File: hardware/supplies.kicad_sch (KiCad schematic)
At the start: 7 parts, among them U301 LM7805_TO220

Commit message: Added analog stage for Vbat measurement, and it's simulation
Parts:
- F301: footprint Fuse:Fuse_1812_4532Metric_Pad1.30x3.40mm_HandSolder -> Fuse:Fuse_1206_3216Metric_Pad1.42x1.75mm_HandSolder
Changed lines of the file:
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@@
     (property "Reference" "F301" (id 0) (at 119.38 95.8682 90))
     (property "Value" "Fuse" (id 1) (at 119.38 98.4051 90))
-    (property "Footprint" "Fuse:Fuse_1812_4532Metric_Pad1.30x3.40mm_HandSolder" (id 2) (at 119.38 102.108 90)
+    (property "Footprint" "Fuse:Fuse_1206_3216Metric_Pad1.42x1.75mm_HandSolder" (id 2) (at 119.38 102.108 90)
       (effects (font (size 1.27 1.27)) hide)
     )

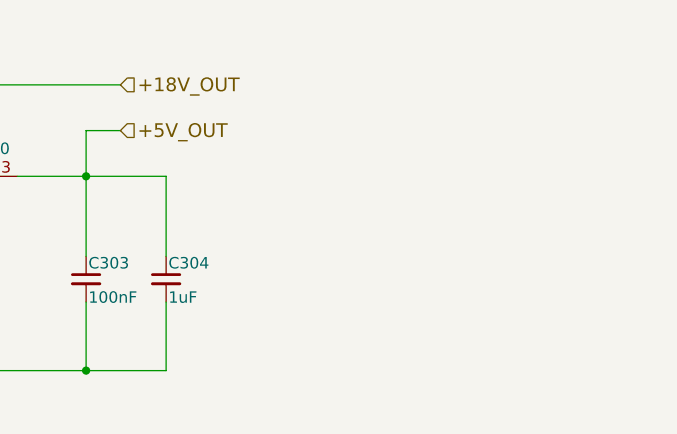
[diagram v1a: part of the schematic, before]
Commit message: hardware: K78L15 to supply INA826 and other changes
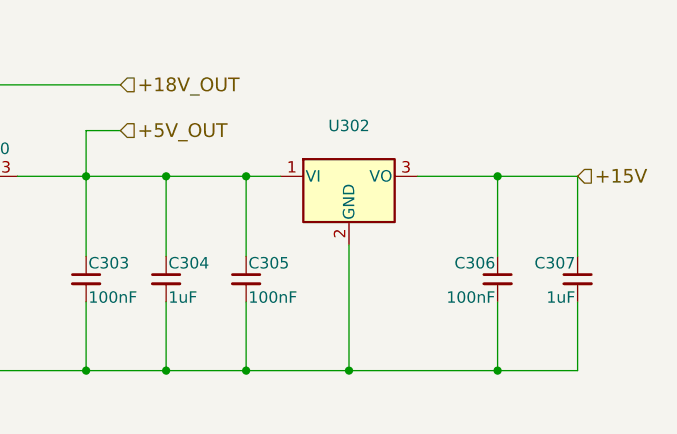
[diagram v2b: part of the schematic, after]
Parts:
- added C305, C306: 100nF, Capacitor_SMD:C_0805_2012Metric_Pad1.18x1.45mm_HandSolder, symbol Device:C_Small
- added C307: 1uF, Capacitor_SMD:C_1206_3216Metric_Pad1.33x1.80mm_HandSolder, symbol Device:C_Small
- added U302: (no value), symbol Regulator_Linear:LM7808_TO220
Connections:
- net +5V_OUT: now also C305.1, U302.1 (VI)
- net GND: now also C305.2, C306.2, C307.2, U302.2 (GND)
- new net +15V: C306.1, C307.1, U302.3 (VO)
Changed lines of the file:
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@@
   (junction (at 132.08 100.33) (diameter 0) (color 0 0 0 0)
   )
+  (junction (at 182.88 100.33) (diameter 0) (color 0 0 0 0)
+  )
   (junction (at 165.1 100.33) (diameter 0) (color 0 0 0 0)
   )
   (junction (at 132.08 90.17) (diameter 0) (color 0 0 0 0)
   )
+  (junction (at 173.99 100.33) (diameter 0) (color 0 0 0 0)
+  )
+  (junction (at 182.88 121.92) (diameter 0) (color 0 0 0 0)
+  )
   (junction (at 124.46 121.92) (diameter 0) (color 0 0 0 0)
   )
+  (junction (at 210.82 121.92) (diameter 0) (color 0 0 0 0)
+  )
   (junction (at 132.08 121.92) (diameter 0) (color 0 0 0 0)
   )
+  (junction (at 210.82 100.33) (diameter 0) (color 0 0 0 0)
+  )
+  (junction (at 173.99 121.92) (diameter 0) (color 0 0 0 0)
+  )
+  (junction (at 194.31 121.92) (diameter 0) (color 0 0 0 0)
+  )
   (junction (at 165.1 121.92) (diameter 0) (color 0 0 0 0)
   )
+  (wire (pts (xy 201.93 100.33) (xy 210.82 100.33))
+    (stroke (width 0) (type default) (color 0 0 0 0))
+  )
+  (wire (pts (xy 182.88 121.92) (xy 194.31 121.92))
+    (stroke (width 0) (type default) (color 0 0 0 0))
+  )
   (wire (pts (xy 132.08 100.33) (xy 132.08 109.22))
     (stroke (width 0) (type default) (color 0 0 0 0))
   )
+  (wire (pts (xy 182.88 109.22) (xy 182.88 100.33))
+    (stroke (width 0) (type default) (color 0 0 0 0))
+  )
+  (wire (pts (xy 182.88 100.33) (xy 186.69 100.33))
+    (stroke (width 0) (type default) (color 0 0 0 0))
+  )
   (wire (pts (xy 165.1 121.92) (xy 173.99 121.92))
     (stroke (width 0) (type default) (color 0 0 0 0))
   )
+  (wire (pts (xy 194.31 121.92) (xy 210.82 121.92))
+    (stroke (width 0) (type default) (color 0 0 0 0))
+  )
   (wire (pts (xy 165.1 100.33) (xy 165.1 109.22))
     (stroke (width 0) (type default) (color 0 0 0 0))
@@
     (stroke (width 0) (type default) (color 0 0 0 0))
   )
+  (wire (pts (xy 210.82 114.3) (xy 210.82 121.92))
+    (stroke (width 0) (type default) (color 0 0 0 0))
+  )
   (wire (pts (xy 165.1 121.92) (xy 165.1 114.3))
     (stroke (width 0) (type default) (color 0 0 0 0))
   )
+  (wire (pts (xy 219.71 100.33) (xy 210.82 100.33))
+    (stroke (width 0) (type default) (color 0 0 0 0))
+  )
+  (wire (pts (xy 210.82 121.92) (xy 219.71 121.92))
+    (stroke (width 0) (type default) (color 0 0 0 0))
+  )
   (wire (pts (xy 165.1 95.25) (xy 165.1 100.33))
     (stroke (width 0) (type default) (color 0 0 0 0))
   )
+  (wire (pts (xy 210.82 100.33) (xy 210.82 109.22))
+    (stroke (width 0) (type default) (color 0 0 0 0))
+  )
   (wire (pts (xy 124.46 100.33) (xy 124.46 109.22))
     (stroke (width 0) (type default) (color 0 0 0 0))
   )
+  (wire (pts (xy 182.88 121.92) (xy 182.88 114.3))
+    (stroke (width 0) (type default) (color 0 0 0 0))
+  )
   (wire (pts (xy 115.57 100.33) (xy 113.03 100.33))
     (stroke (width 0) (type default) (color 0 0 0 0))
@@
     (stroke (width 0) (type default) (color 0 0 0 0))
   )
+  (wire (pts (xy 194.31 121.92) (xy 194.31 107.95))
+    (stroke (width 0) (type default) (color 0 0 0 0))
+  )
   (wire (pts (xy 173.99 100.33) (xy 173.99 109.22))
     (stroke (width 0) (type default) (color 0 0 0 0))
   )
+  (wire (pts (xy 173.99 121.92) (xy 182.88 121.92))
+    (stroke (width 0) (type default) (color 0 0 0 0))
+  )
   (wire (pts (xy 149.86 121.92) (xy 149.86 107.95))
     (stroke (width 0) (type default) (color 0 0 0 0))
@@
     (stroke (width 0) (type default) (color 0 0 0 0))
   )
+  (wire (pts (xy 182.88 100.33) (xy 173.99 100.33))
+    (stroke (width 0) (type default) (color 0 0 0 0))
+  )
   (wire (pts (xy 105.41 100.33) (xy 100.33 100.33))
     (stroke (width 0) (type default) (color 0 0 0 0))
@@
     (stroke (width 0) (type default) (color 0 0 0 0))
   )
+  (wire (pts (xy 219.71 121.92) (xy 219.71 114.3))
+    (stroke (width 0) (type default) (color 0 0 0 0))
+  )
   (wire (pts (xy 168.91 95.25) (xy 165.1 95.25))
     (stroke (width 0) (type default) (color 0 0 0 0))
@@
     (stroke (width 0) (type default) (color 0 0 0 0))
   )
+  (wire (pts (xy 219.71 109.22) (xy 219.71 100.33))
+    (stroke (width 0) (type default) (color 0 0 0 0))
+  )
   (wire (pts (xy 132.08 87.63) (xy 132.08 90.17))
     (stroke (width 0) (type default) (color 0 0 0 0))
@@
   (wire (pts (xy 132.08 90.17) (xy 168.91 90.17))
     (stroke (width 0) (type default) (color 0 0 0 0))
+  )
+  (hierarchical_label "+15V" (shape input) (at 219.71 100.33 0)
+    (effects (font (size 1.524 1.524)) (justify left))
   )
   (hierarchical_label "+18V_IN" (shape input) (at 100.33 100.33 180)
@@
     )
     (pin "1")
+  )
+  (symbol (lib_id "Device:C_Small") (at 210.82 111.76 0) (mirror y) (unit 1)
+    (in_bom yes) (on_board yes)
+    (property "Reference" "C306" (id 0) (at 210.566 109.982 0)
+      (effects (font (size 1.27 1.27)) (justify left))
+    )
+    (property "Value" "100nF" (id 1) (at 210.566 113.792 0)
+      (effects (font (size 1.27 1.27)) (justify left))
+    )
+    (property "Footprint" "Capacitor_SMD:C_0805_2012Metric_Pad1.18x1.45mm_HandSolder" (id 2) (at 210.82 111.76 0)
+      (effects (font (size 1.27 1.27)) hide)
+    )
+    (property "Datasheet" "" (id 3) (at 210.82 111.76 0)
+      (effects (font (size 1.27 1.27)) hide)
+    )
+    (pin "1")
+    (pin "2")
+  )
+  (symbol (lib_id "Regulator_Linear:LM7808_TO220") (at 194.31 100.33 0) (unit 1)
+    (in_bom yes) (on_board yes) (fields_autoplaced)
+    (property "Reference" "U302" (id 0) (at 194.31 94.7252 0))
+    (property "Value" "" (id 1) (at 194.31 97.2621 0))
+    (property "Footprint" "" (id 2) (at 194.31 94.615 0)
+      (effects (font (size 1.27 1.27) italic) hide)
+    )
+    (property "Datasheet" "https://www.onsemi.cn/PowerSolutions/document/MC7800-D.PDF" (id 3) (at 194.31 101.6 0)
+      (effects (font (size 1.27 1.27)) hide)
+    )
+    (pin "1")
+    (pin "2")
+    (pin "3")
   )
   (symbol (lib_id "Device:Fuse") (at 119.38 100.33 90) (unit 1)
@@
       (effects (font (size 1.27 1.27)) hide)
     )
+    (pin "1")
+    (pin "2")
+  )
+  (symbol (lib_id "Device:C_Small") (at 182.88 111.76 0) (unit 1)
+    (in_bom yes) (on_board yes)
+    (property "Reference" "C305" (id 0) (at 183.134 109.982 0)
+      (effects (font (size 1.27 1.27)) (justify left))
+    )
+    (property "Value" "100nF" (id 1) (at 183.134 113.792 0)
+      (effects (font (size 1.27 1.27)) (justify left))
+    )
+    (property "Footprint" "Capacitor_SMD:C_0805_2012Metric_Pad1.18x1.45mm_HandSolder" (id 2) (at 182.88 111.76 0)
+      (effects (font (size 1.27 1.27)) hide)
+    )
+    (property "Datasheet" "" (id 3) (at 182.88 111.76 0)
+      (effects (font (size 1.27 1.27)) hide)
+    )
+    (pin "1")
+    (pin "2")
+  )
+  (symbol (lib_id "Device:C_Small") (at 219.71 111.76 0) (mirror y) (unit 1)
+    (in_bom yes) (on_board yes)
+    (property "Reference" "C307" (id 0) (at 219.456 109.982 0)
+      (effects (font (size 1.27 1.27)) (justify left))
+    )
+    (property "Value" "1uF" (id 1) (at 219.456 113.792 0)
+      (effects (font (size 1.27 1.27)) (justify left))
+    )
+    (property "Footprint" "Capacitor_SMD:C_1206_3216Metric_Pad1.33x1.80mm_HandSolder" (id 2) (at 219.71 111.76 0)
+      (effects (font (size 1.27 1.27)) hide)
+    )
+    (property "Datasheet" "" (id 3) (at 219.71 111.76 0)
+      (effects (font (size 1.27 1.27)) hide)
+    )

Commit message: hardware: silkscreen updated with JLC. Finished.
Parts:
- added C308: 1uF, Capacitor_SMD:C_1206_3216Metric_Pad1.33x1.80mm_HandSolder, symbol Device:C_Small
- U302: value (none) -> K78L15-1000R3; footprint (none) -> KicadZeniteSolarLibrary18:TO-220-3_Horizontal_TabDown_SMD
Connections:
- net +18V_OUT: now also C305.1, U302.1 (VI), C308.1
- net +5V_OUT: no longer C305.1, U302.1 (VI)
- net GND: now also C308.2
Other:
- moved on the sheet: C304, C305, C306, C307, D301, F301, U302
